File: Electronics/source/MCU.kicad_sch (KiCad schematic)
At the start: 70 parts, among them J1 Conn_01x05, J16 Conn_01x02, J2 Conn_01x03, J22 Conn_01x04, J3 Conn_01x03, J4 Conn_01x05, J6 Conn_01x20, J7 Conn_01x20, SW10 SW_Push, SW11 SW_Push, SW12 SW_Push, SW13 SW_Push, SW14 SW_Coded, SW4 SW_Push, SW5 SW_SPDT, SW6 SW_SPDT, SW7 SW_SPDT, SW8 SW_Push, SW9 SW_Push, U1 STM32F072CBTx, U4 LM2902, U5 ADP122AUJZ-3.3-R7, Y1 ABL-8.000MHZ-B2

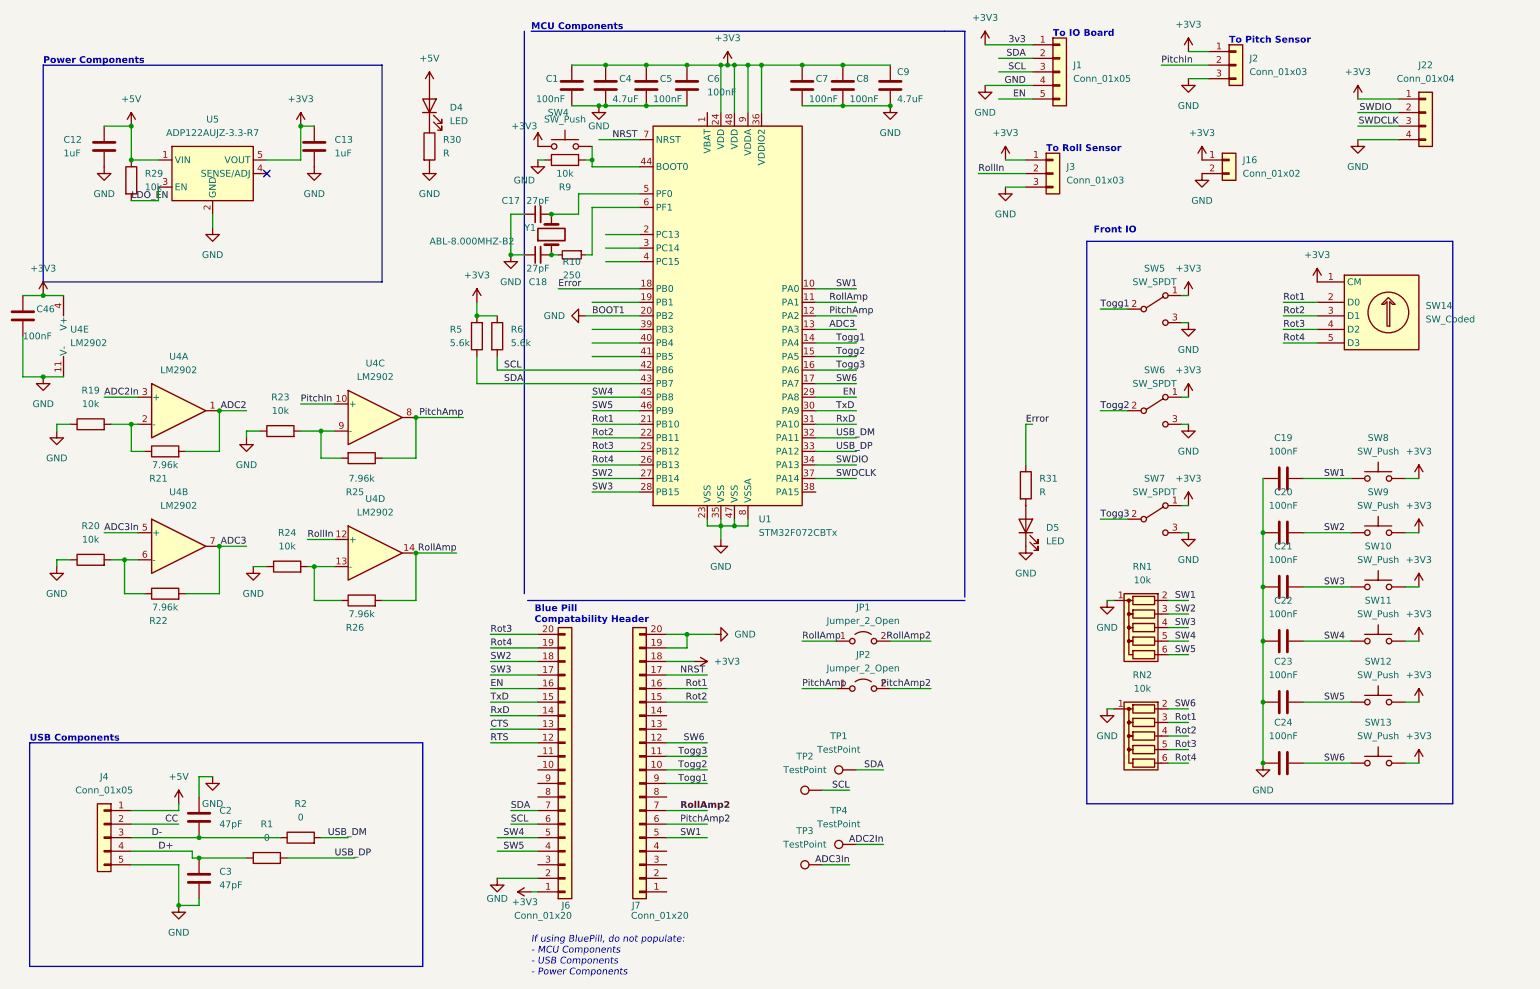
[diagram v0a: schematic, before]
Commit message: implemented MCP6004/9 and rerouted
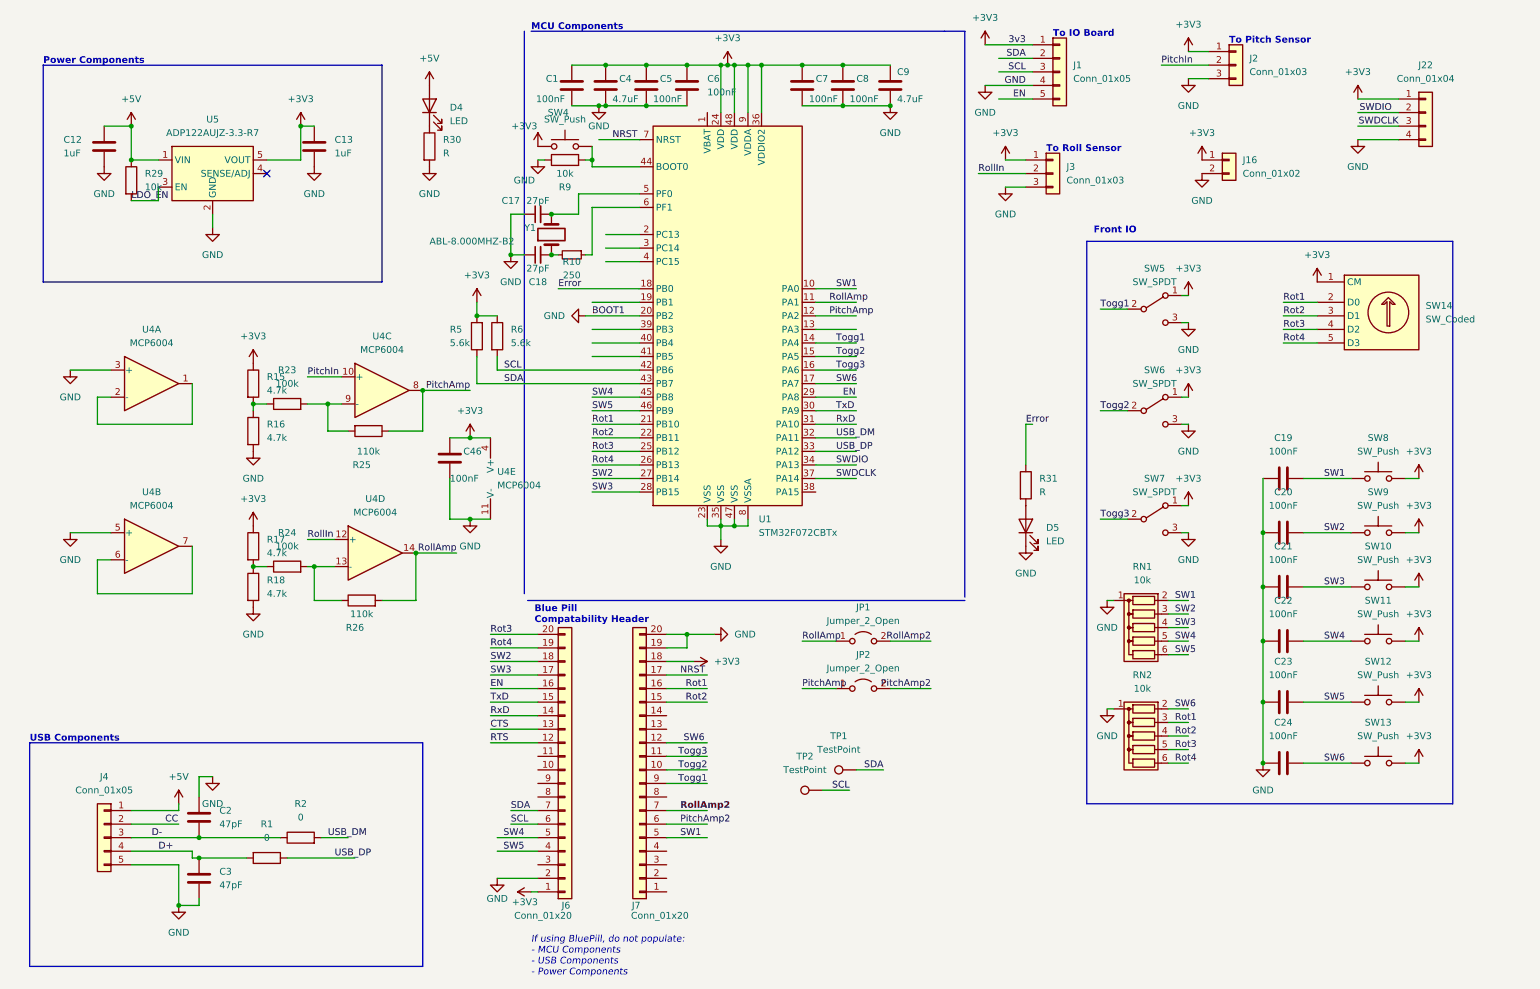
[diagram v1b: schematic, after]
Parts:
- removed R19, R20: 10k, Resistor_SMD:R_0603_1608Metric, symbol Device:R
- removed R21, R22: 7.96k, Resistor_SMD:R_0603_1608Metric, symbol Device:R
- removed TP3, TP4: TestPoint, TestPoint:TestPoint_Pad_D1.0mm, symbol Connector:TestPoint
- removed U4: LM2902, Package_SO:TSSOP-14_4.4x5mm_P0.65mm, symbol Amplifier_Operational:LM2902
- added R15, R16, R17, R18: 4.7k, Resistor_SMD:R_0603_1608Metric, symbol Device:R
- added U4: MCP6004, Package_SO:TSSOP-14_4.4x5mm_P0.65mm, symbol Amplifier_Operational:MCP6004
- R23, R24: value 10k -> 100k
- R25, R26: value 7.96k -> 110k
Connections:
- net +3V3: now also R15.1, R17.1, U4.4 (V+)
- net GND: now also R16.2, R18.2, U4.11 (V-), U4.3 (+), U4.5 (+); no longer R23.1, R24.1
- net PitchAmp: now also U4.8
- net PitchIn: now also U4.10 (+)
- net RollAmp: now also U4.14
- net RollIn: now also U4.12 (+)
- net at R23.2, R25.2: now also U4.9 (-)
- net at R24.2, R26.1: now also U4.13 (-)
- net ADC3: no longer names the net of U1.13 (PA3)
- new net: R15.2, R16.1, R23.1
- new net: U4.6 (-), U4.7
- new net: R17.2, R18.1, R24.1
- new net: U4.1, U4.2 (-)
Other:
- moved on the sheet: C46, R23, R25

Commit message: Redefined face shape to fit panel mount hat; rerouted; DRC check
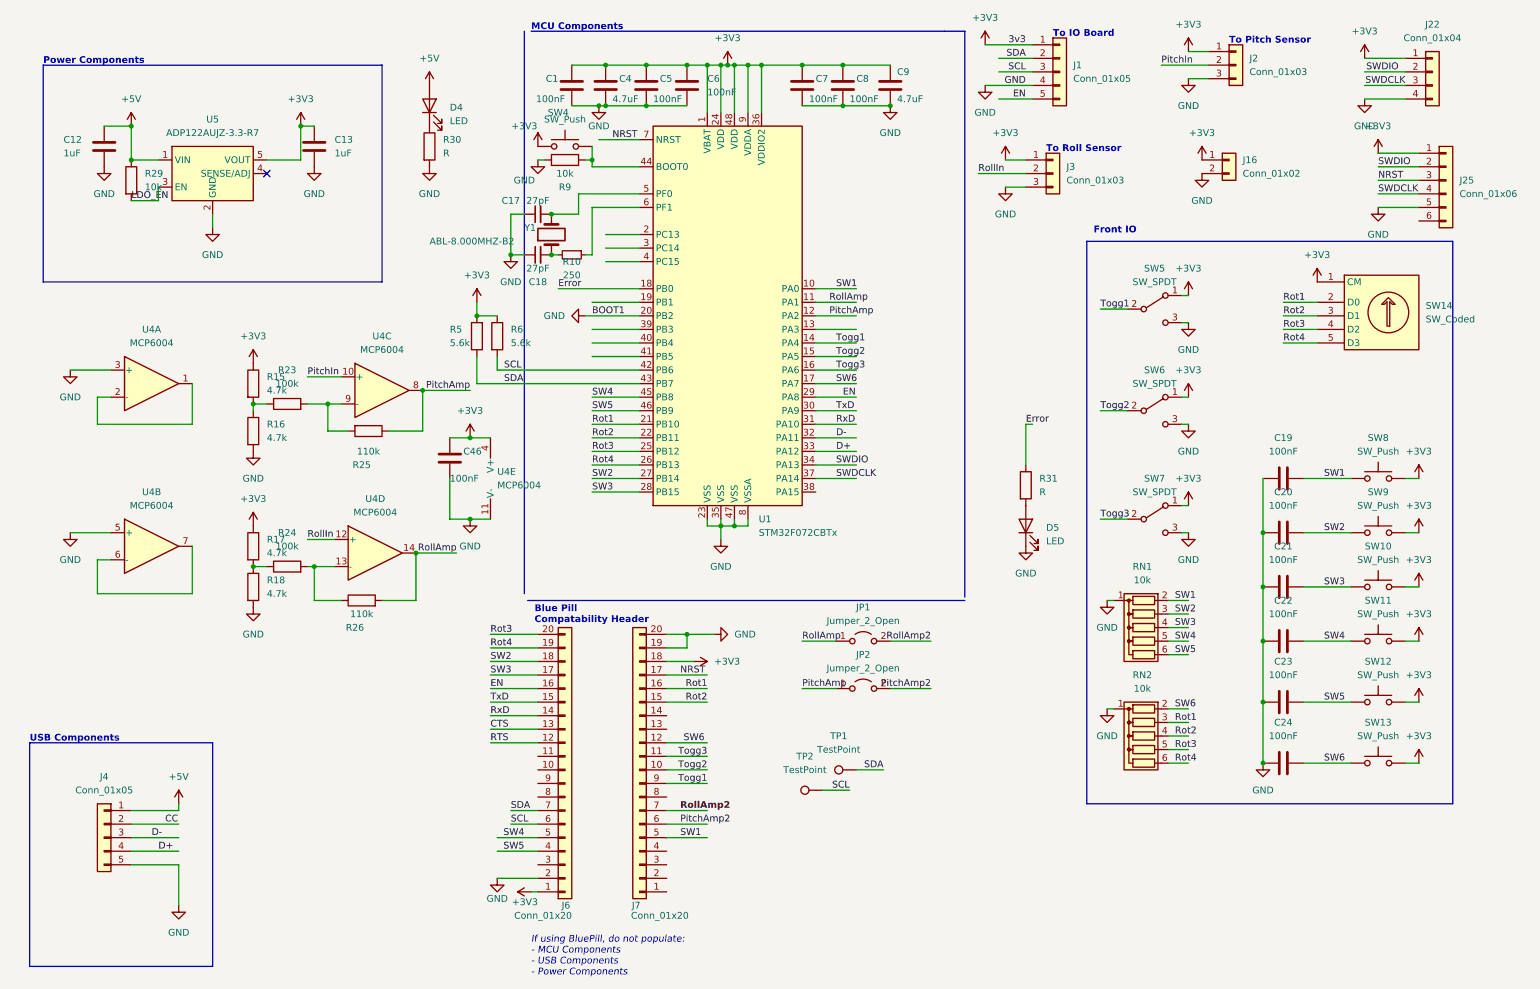
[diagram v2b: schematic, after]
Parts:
- removed C2, C3: 47pF, Capacitor_SMD:C_0805_2012Metric, symbol Device:C
- removed R1, R2: 0, Resistor_SMD:R_0805_2012Metric, symbol Device:R
- added J25: Conn_01x06, Connector:Tag-Connect_TC2030-IDC-NL_2x03_P1.27mm_Vertical, symbol Connector_Generic:Conn_01x06
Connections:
- net USB_DP is gone; now on net D+: U1.33 (PA12)
- net +3V3: now also U1.1 (VBAT), J25.1 (Pin_1)
- net GND: now also J25.5 (Pin_5)
- net NRST: now also J25.3 (Pin_3)
- net SWDCLK: now also J25.4 (Pin_4)
- net SWDIO: now also J25.2 (Pin_2)
- net USB_DM renamed D-
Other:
- moved on the sheet: J22
